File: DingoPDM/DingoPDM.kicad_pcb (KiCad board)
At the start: 4 copper layers, 72.4 x 95.2 mm, 152 parts, among them J1 RedCubeTerminal, J2 RedCubeTerminal, J3 Conn_01x12, J4 TC, J5 USB_C_Receptacle_USB2.0, SW1 BOOT, U1 VXO780x-500-M, U10 BTS7008-2EPA, U11 BTS7008-2EPA, U12 LM324, U13 BTS7008-2EPA, U2 LD1117S33CTR, U3 PCA82C250, U4 STM32F446RETx, U5 MB85RC256V, U6 MCP9808, U7 LM324, U8 BTS700n-1EPP, U9 BTS700n-1EPP, Y1 8mHz

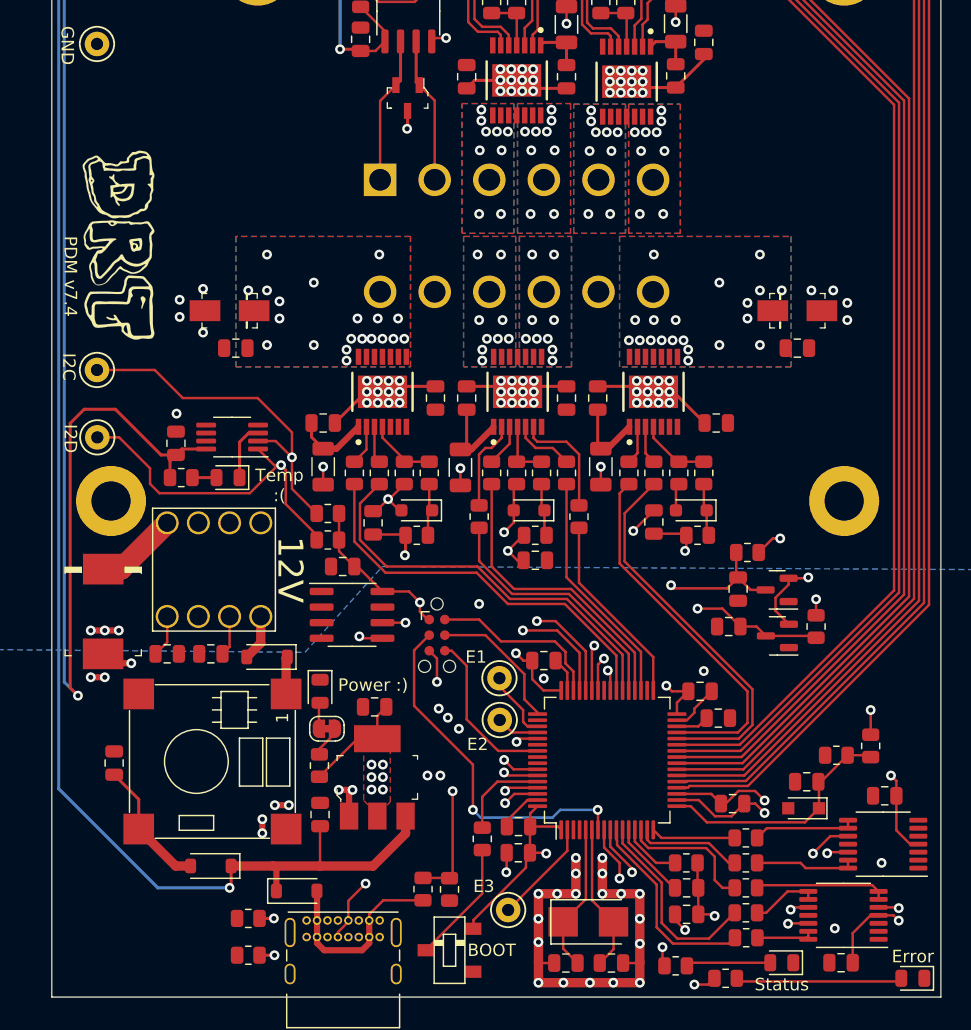
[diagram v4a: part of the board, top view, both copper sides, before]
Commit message: docs - add to firmware
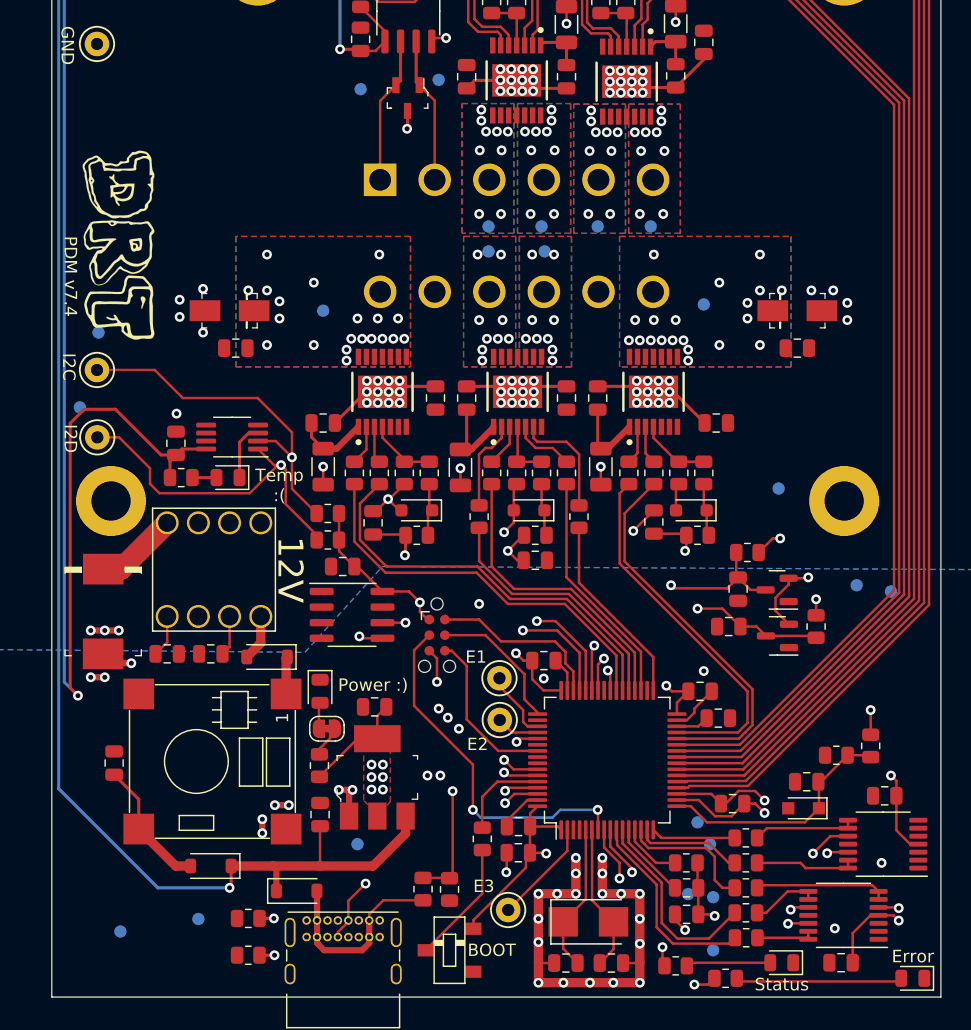
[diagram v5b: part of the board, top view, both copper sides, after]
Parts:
- added TP11: OUT2, TestPoint:TestPoint_Pad_D1.0mm, B.Cu at (-15.7, 6.10)
- added TP12: IN2, TestPoint:TestPoint_Pad_D1.0mm, B.Cu at (27.7, 28.4)
- added TP13: OUT3, TestPoint:TestPoint_Pad_D1.0mm, B.Cu at (-2.29, 1.27)
- added TP14: OUT4, TestPoint:TestPoint_Pad_D1.0mm, B.Cu at (2.29, 1.27)
- added TP15: IN1, TestPoint:TestPoint_Pad_D1.0mm, B.Cu at (21.3, 20.6)
- added TP16: OUT1, TestPoint:TestPoint_Pad_D1.0mm, B.Cu at (15.2, 5.59)
- added TP17: OUT5, TestPoint:TestPoint_Pad_D1.0mm, B.Cu at (10.9, -0.76)
- added TP18: OUT6, TestPoint:TestPoint_Pad_D1.0mm, B.Cu at (6.60, -0.76)
- added TP19: OUT7, TestPoint:TestPoint_Pad_D1.0mm, B.Cu at (2.03, -0.76)
- added TP20: OUT8, TestPoint:TestPoint_Pad_D1.0mm, B.Cu at (-2.29, -0.76)
- added TP21: CAN_H, TestPoint:TestPoint_Pad_D1.0mm, B.Cu at (-6.35, -12.7)
- added TP22: CAN_L, TestPoint:TestPoint_Pad_D1.0mm, B.Cu at (-12.7, -11.9)
- added TP23: 12V, TestPoint:TestPoint_Pad_D1.0mm, B.Cu at (30.5, 29.0)
- added TP24: GND, TestPoint:TestPoint_Pad_D1.0mm, B.Cu at (-32.3, 56.6)
- added TP25: I2C1_SCL, TestPoint:TestPoint_Pad_D1.0mm, B.Cu at (-34.0, 7.87)
- added TP26: I2C1_SDA, TestPoint:TestPoint_Pad_D1.0mm, B.Cu at (-35.6, 14.0)
- added TP27: IS1, TestPoint:TestPoint_Pad_D1.0mm, B.Cu at (14.0, 53.6)
- added TP28: IS2, TestPoint:TestPoint_Pad_D1.0mm, B.Cu at (16.0, 58.2)
- added TP29: IS3_4, TestPoint:TestPoint_Pad_D1.0mm, B.Cu at (16.0, 53.8)
- added TP30: IS5_6, TestPoint:TestPoint_Pad_D1.0mm, B.Cu at (15.7, 49.5)
- added TP31: IS7_8, TestPoint:TestPoint_Pad_D1.0mm, B.Cu at (14.7, 47.8)
- added TP4: 5V, TestPoint:TestPoint_Pad_D1.0mm, B.Cu at (-25.9, 55.6)
- added TP7: 3.3V, TestPoint:TestPoint_Pad_D1.0mm, B.Cu at (-13.0, 49.5)

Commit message: undo accidental changes to kicad
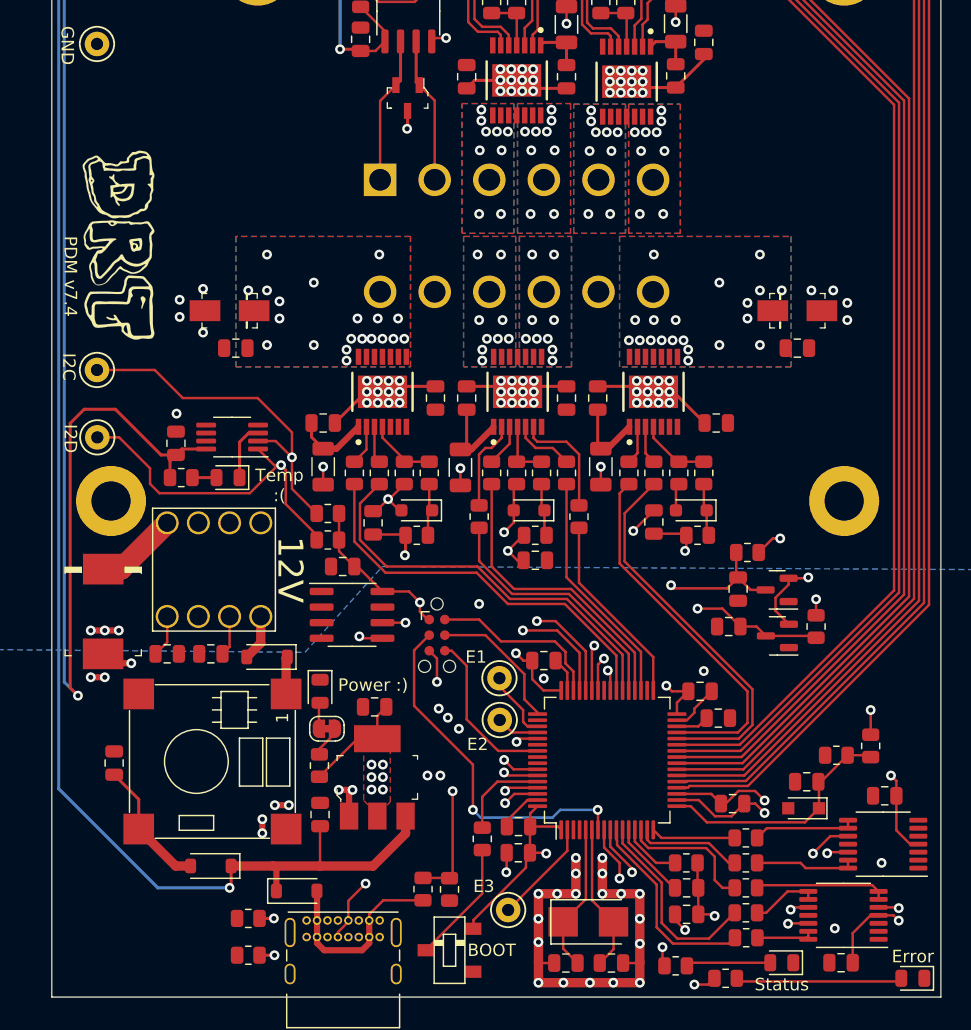
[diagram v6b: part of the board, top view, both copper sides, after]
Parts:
- removed TP11: OUT2, TestPoint:TestPoint_Pad_D1.0mm
- removed TP12: IN2, TestPoint:TestPoint_Pad_D1.0mm
- removed TP13: OUT3, TestPoint:TestPoint_Pad_D1.0mm
- removed TP14: OUT4, TestPoint:TestPoint_Pad_D1.0mm
- removed TP15: IN1, TestPoint:TestPoint_Pad_D1.0mm
- removed TP16: OUT1, TestPoint:TestPoint_Pad_D1.0mm
- removed TP17: OUT5, TestPoint:TestPoint_Pad_D1.0mm
- removed TP18: OUT6, TestPoint:TestPoint_Pad_D1.0mm
- removed TP19: OUT7, TestPoint:TestPoint_Pad_D1.0mm
- removed TP20: OUT8, TestPoint:TestPoint_Pad_D1.0mm
- removed TP21: CAN_H, TestPoint:TestPoint_Pad_D1.0mm
- removed TP22: CAN_L, TestPoint:TestPoint_Pad_D1.0mm
- removed TP23: 12V, TestPoint:TestPoint_Pad_D1.0mm
- removed TP24: GND, TestPoint:TestPoint_Pad_D1.0mm
- removed TP25: I2C1_SCL, TestPoint:TestPoint_Pad_D1.0mm
- removed TP26: I2C1_SDA, TestPoint:TestPoint_Pad_D1.0mm
- removed TP27: IS1, TestPoint:TestPoint_Pad_D1.0mm
- removed TP28: IS2, TestPoint:TestPoint_Pad_D1.0mm
- removed TP29: IS3_4, TestPoint:TestPoint_Pad_D1.0mm
- removed TP30: IS5_6, TestPoint:TestPoint_Pad_D1.0mm
- removed TP31: IS7_8, TestPoint:TestPoint_Pad_D1.0mm
- removed TP4: 5V, TestPoint:TestPoint_Pad_D1.0mm
- removed TP7: 3.3V, TestPoint:TestPoint_Pad_D1.0mm
